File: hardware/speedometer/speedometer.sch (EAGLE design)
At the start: 123 parts, among them IC1 PIC32MX274F256DT-I_PT, IC10 24LC024SN, IC11 MAX16054AZT+T, IC12 TPS63001DRCT, IC13 TPS63002DRCT, IC2 CSTCE8M00G55-R0, IC3 BQ27441DRZR-G1A, IC7 BQ24075RGTT, IC8 NRF24L01P-T, IC9 CSTCE16M0V53-R0, J1 10104111-0001LF, J2 BAT, J3 CONUFL001-SMD-T, J4 Right_sens, J5 Right, J6 Left_sens, J7 Left, Q1 BC817, Q2 BC817, Q3 BC817, Q4 BC817

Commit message: Minor stuff
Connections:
- removed net UDB_ID: IC1.TMS/RPB5/USBID/RB5
- net USB_ID: now also IC1.TMS/RPB5/USBID/RB5
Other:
- note added: "Short to boot in bootloader mode"
- moved on the sheet: JP3, R14
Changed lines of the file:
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@@
 <text x="20.32" y="86.36" size="1.778" layer="91" font="vector" rot="R90">ESR &lt;= 3 Ohm</text>
 <text x="129.54" y="38.1" size="3.81" layer="91" font="vector">5V Tolerant</text>
+<text x="73.66" y="38.1" size="3.81" layer="91">Short to boot in
+bootloader mode</text>
 </plain>
 <instances>
@@
 <instance part="GND4" gate="1" x="63.5" y="55.88"/>
 <instance part="+3V4" gate="G$1" x="38.1" y="93.98" rot="R90"/>
-<instance part="+3V7" gate="G$1" x="38.1" y="73.66" rot="R90"/>
+<instance part="+3V7" gate="G$1" x="25.4" y="73.66" rot="R90"/>
 <instance part="+3V8" gate="G$1" x="231.14" y="106.68" rot="R270"/>
 <instance part="+3V9" gate="G$1" x="215.9" y="73.66" rot="R270"/>
@@
 <instance part="JP2" gate="A" x="149.86" y="27.94"/>
 <instance part="GND19" gate="1" x="139.7" y="17.78"/>
-<instance part="JP3" gate="G$1" x="121.92" y="27.94"/>
-<instance part="+3V14" gate="G$1" x="111.76" y="40.64"/>
-<instance part="R14" gate="G$1" x="104.14" y="22.86"/>
-<instance part="GND20" gate="1" x="96.52" y="17.78"/>
+<instance part="JP3" gate="G$1" x="109.22" y="27.94"/>
+<instance part="+3V14" gate="G$1" x="99.06" y="35.56"/>
+<instance part="R14" gate="G$1" x="91.44" y="22.86"/>
+<instance part="GND20" gate="1" x="83.82" y="17.78"/>
 </instances>
 <busses>
@@
 <segment>
 <pinref part="R14" gate="G$1" pin="1"/>
-<wire x1="99.06" y1="22.86" x2="96.52" y2="22.86" width="0.1524" layer="91"/>
-<wire x1="96.52" y1="22.86" x2="96.52" y2="20.32" width="0.1524" layer="91"/>
+<wire x1="86.36" y1="22.86" x2="83.82" y2="22.86" width="0.1524" layer="91"/>
+<wire x1="83.82" y1="22.86" x2="83.82" y2="20.32" width="0.1524" layer="91"/>
 <pinref part="GND20" gate="1" pin="GND"/>
 </segment>
@@
 <pinref part="+3V7" gate="G$1" pin="+3V3"/>
 <pinref part="IC1" gate="G$1" pin="AVDD"/>
-<wire x1="40.64" y1="73.66" x2="66.04" y2="73.66" width="0.1524" layer="91"/>
+<wire x1="27.94" y1="73.66" x2="66.04" y2="73.66" width="0.1524" layer="91"/>
 </segment>
 <segment>
@@
 <segment>
 <pinref part="JP3" gate="G$1" pin="1"/>
-<wire x1="119.38" y1="30.48" x2="114.3" y2="30.48" width="0.1524" layer="91"/>
-<wire x1="114.3" y1="30.48" x2="111.76" y2="30.48" width="0.1524" layer="91"/>
-<wire x1="111.76" y1="30.48" x2="111.76" y2="38.1" width="0.1524" layer="91"/>
+<wire x1="106.68" y1="30.48" x2="101.6" y2="30.48" width="0.1524" layer="91"/>
+<wire x1="101.6" y1="30.48" x2="99.06" y2="30.48" width="0.1524" layer="91"/>
+<wire x1="99.06" y1="30.48" x2="99.06" y2="33.02" width="0.1524" layer="91"/>
 <pinref part="+3V14" gate="G$1" pin="+3V3"/>
 </segment>
@@
 <label x="104.14" y="154.94" size="1.27" layer="95" font="vector" rot="R180" xref="yes"/>
 </segment>
-</net>
-<net name="UDB_ID" class="0">
 <segment>
 <pinref part="IC1" gate="G$1" pin="TMS/RPB5/USBID/RB5"/>
@@
 <segment>
 <pinref part="JP3" gate="G$1" pin="2"/>
-<wire x1="119.38" y1="27.94" x2="111.76" y2="27.94" width="0.1524" layer="91"/>
-<label x="93.98" y="27.94" size="1.27" layer="95" font="vector" rot="R180" xref="yes"/>
+<wire x1="106.68" y1="27.94" x2="99.06" y2="27.94" width="0.1524" layer="91"/>
+<label x="81.28" y="27.94" size="1.27" layer="95" font="vector" rot="R180" xref="yes"/>
 <pinref part="R14" gate="G$1" pin="2"/>
-<wire x1="111.76" y1="27.94" x2="93.98" y2="27.94" width="0.1524" layer="91"/>
-<wire x1="109.22" y1="22.86" x2="111.76" y2="22.86" width="0.1524" layer="91"/>
-<wire x1="111.76" y1="22.86" x2="111.76" y2="27.94" width="0.1524" layer="91"/>
-<junction x="111.76" y="27.94"/>
-</segment>
-</net>
+<wire x1="99.06" y1="27.94" x2="81.28" y2="27.94" width="0.1524" layer="91"/>
+<wire x1="96.52" y1="22.86" x2="99.06" y2="22.86" width="0.1524" layer="91"/>
+<wire x1="99.06" y1="22.86" x2="99.06" y2="27.94" width="0.1524" layer="91"/>
+<junction x="99.06" y="27.94"/>
+</segment>
+</net>

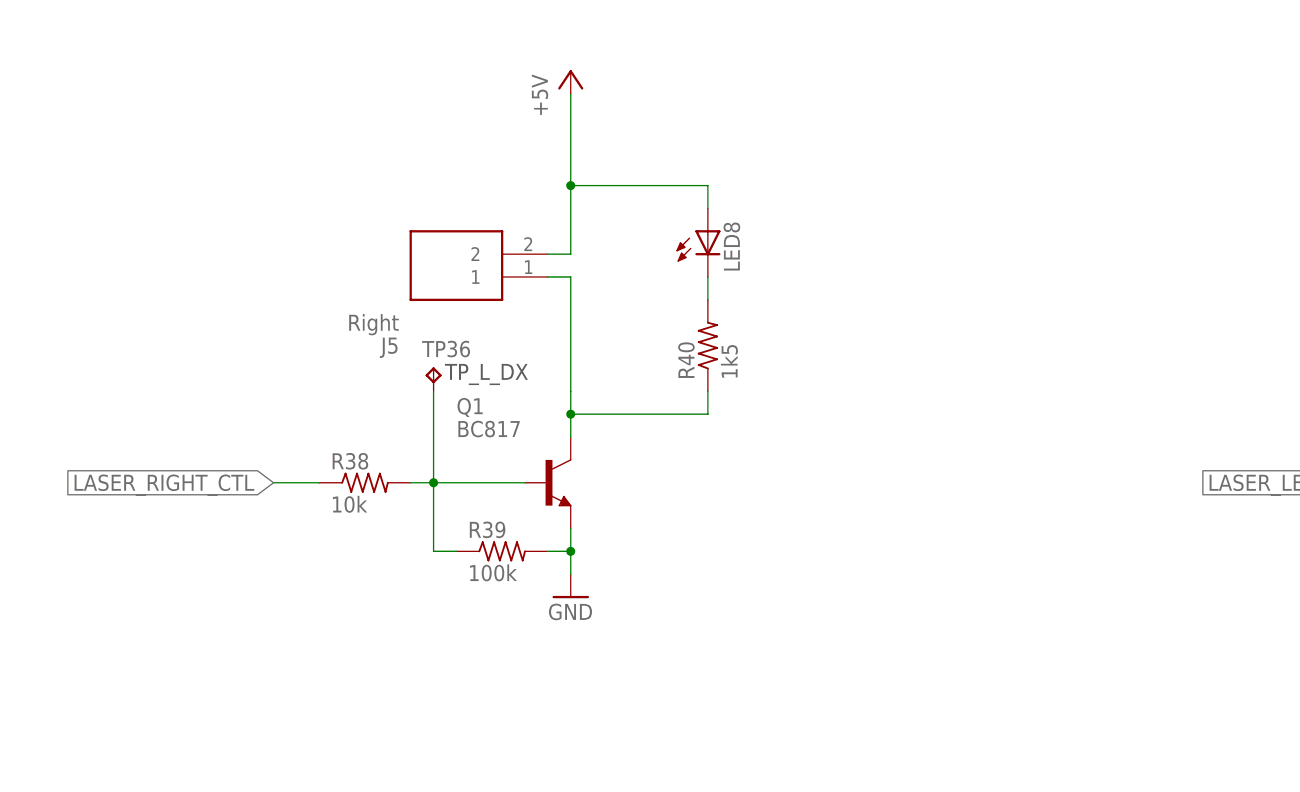
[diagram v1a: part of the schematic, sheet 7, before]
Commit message: Laser ctl logic added
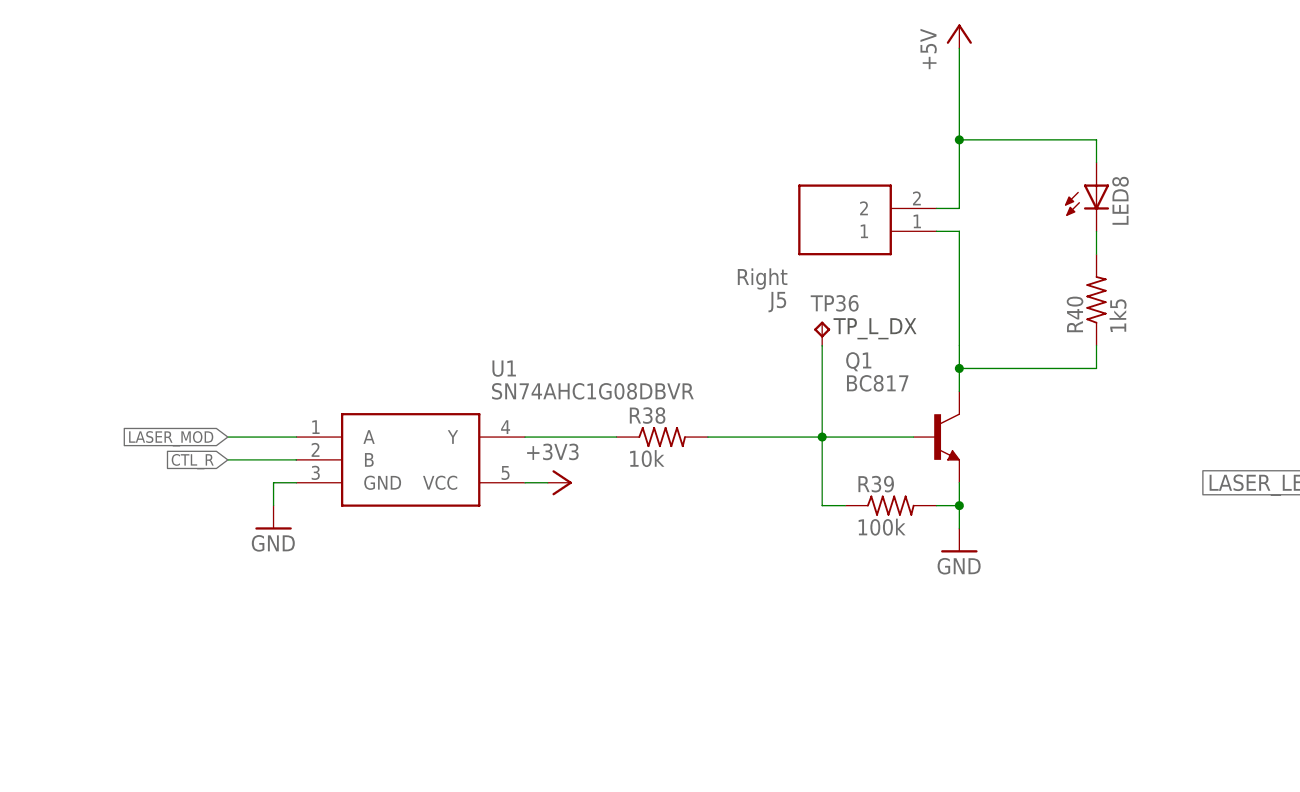
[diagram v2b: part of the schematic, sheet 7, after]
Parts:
- added U1: SN74AHC1G08DBVR, SN74AHC1G08DBVR:SN74AHC1G08DBVR
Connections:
- removed net LASER_RIGHT_CTL: R38.1
- new net LASER_MOD: IC1.RPC7/PMCS1/RC7, U1.A
- new net N$42: R38.1, U1.Y
- net +3V3: now also U1.VCC
- net CTL_R: now also U1.B
- net GND: now also U1.GND
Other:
- moved on the sheet: J5, LED8, Q1, R38, R39, R40, TP36
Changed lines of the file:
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@@
 <part name="R14" library="rcl" library_urn="urn:adsk.eagle:library:334" deviceset="R-US_" device="M0805" package3d_urn="urn:adsk.eagle:package:23556/1" value="10k"/>
 <part name="GND20" library="supply1" library_urn="urn:adsk.eagle:library:371" deviceset="GND" device=""/>
+<part name="U1" library="SN74AHC1G08DBVR" deviceset="SN74AHC1G08DBVR" device=""/>
+<part name="GND21" library="supply1" library_urn="urn:adsk.eagle:library:371" deviceset="GND" device=""/>
+<part name="+3V15" library="supply1" library_urn="urn:adsk.eagle:library:371" deviceset="+3V3" device=""/>
 </parts>
 <sheets>
@@
 </segment>
 </net>
+<net name="LASER_MOD" class="0">
+<segment>
+<pinref part="IC1" gate="G$1" pin="RPC7/PMCS1/RC7"/>
+<wire x1="66.04" y1="111.76" x2="53.34" y2="111.76" width="0.1524" layer="91"/>
+<label x="53.34" y="111.76" size="1.27" layer="95" font="vector" rot="R180" xref="yes"/>
+</segment>
+</net>
 </nets>
 </sheet>
@@
 <instances>
 <instance part="FRAME9" gate="G$1" x="0" y="0"/>
-<instance part="Q1" gate="G$1" x="66.04" y="114.3"/>
-<instance part="GND67" gate="1" x="68.58" y="101.6"/>
-<instance part="R38" gate="G$1" x="45.72" y="114.3"/>
-<instance part="R39" gate="G$1" x="60.96" y="106.68"/>
-<instance part="TP36" gate="G$1" x="53.34" y="127"/>
-<instance part="LED8" gate="G$1" x="83.82" y="142.24"/>
-<instance part="R40" gate="G$1" x="83.82" y="129.54" rot="R90"/>
-<instance part="J5" gate="G$1" x="66.04" y="137.16" rot="R180"/>
+<instance part="Q1" gate="G$1" x="109.22" y="119.38"/>
+<instance part="GND67" gate="1" x="111.76" y="106.68"/>
+<instance part="R38" gate="G$1" x="78.74" y="119.38"/>
+<instance part="R39" gate="G$1" x="104.14" y="111.76"/>
+<instance part="TP36" gate="G$1" x="96.52" y="132.08"/>
+<instance part="LED8" gate="G$1" x="127" y="147.32"/>
+<instance part="R40" gate="G$1" x="127" y="134.62" rot="R90"/>
+<instance part="J5" gate="G$1" x="109.22" y="142.24" rot="R180"/>
 <instance part="J4" gate="G$1" x="48.26" y="45.72" rot="R180"/>
 <instance part="GND66" gate="1" x="53.34" y="40.64"/>
@@
 <instance part="J6" gate="G$1" x="172.72" y="45.72" rot="R180"/>
 <instance part="GND68" gate="1" x="177.8" y="40.64"/>
-<instance part="P+2" gate="1" x="68.58" y="160.02"/>
+<instance part="P+2" gate="1" x="111.76" y="165.1"/>
 <instance part="P+3" gate="1" x="193.04" y="160.02"/>
 <instance part="P+4" gate="1" x="53.34" y="71.12"/>
@@
 <instance part="R25" gate="G$1" x="218.44" y="60.96" rot="R90"/>
 <instance part="+3V6" gate="G$1" x="218.44" y="71.12"/>
+<instance part="U1" gate="G$1" x="38.1" y="119.38"/>
+<instance part="GND21" gate="1" x="35.56" y="109.22"/>
+<instance part="+3V15" gate="G$1" x="68.58" y="114.3" rot="R270"/>
 </instances>
 <busses>
@@
 <segment>
 <pinref part="Q1" gate="G$1" pin="C"/>
-<wire x1="68.58" y1="119.38" x2="68.58" y2="121.92" width="0.1524" layer="91"/>
-<wire x1="68.58" y1="121.92" x2="68.58" y2="124.46" width="0.1524" layer="91"/>
-<wire x1="68.58" y1="121.92" x2="83.82" y2="121.92" width="0.1524" layer="91"/>
-<junction x="68.58" y="121.92"/>
+<wire x1="111.76" y1="124.46" x2="111.76" y2="127" width="0.1524" layer="91"/>
+<wire x1="111.76" y1="127" x2="111.76" y2="129.54" width="0.1524" layer="91"/>
+<wire x1="111.76" y1="127" x2="127" y2="127" width="0.1524" layer="91"/>
+<junction x="111.76" y="127"/>
 <pinref part="R40" gate="G$1" pin="1"/>
-<wire x1="83.82" y1="121.92" x2="83.82" y2="124.46" width="0.1524" layer="91"/>
+<wire x1="127" y1="127" x2="127" y2="129.54" width="0.1524" layer="91"/>
 <pinref part="J5" gate="G$1" pin="1"/>
-<wire x1="66.04" y1="137.16" x2="68.58" y2="137.16" width="0.1524" layer="91"/>
-<wire x1="68.58" y1="137.16" x2="68.58" y2="124.46" width="0.1524" layer="91"/>
+<wire x1="109.22" y1="142.24" x2="111.76" y2="142.24" width="0.1524" layer="91"/>
+<wire x1="111.76" y1="142.24" x2="111.76" y2="129.54" width="0.1524" layer="91"/>
 </segment>
 </net>
@@
 <pinref part="Q1" gate="G$1" pin="E"/>
 <pinref part="GND67" gate="1" pin="GND"/>
-<wire x1="68.58" y1="109.22" x2="68.58" y2="106.68" width="0.1524" layer="91"/>
+<wire x1="111.76" y1="114.3" x2="111.76" y2="111.76" width="0.1524" layer="91"/>
 <pinref part="R39" gate="G$1" pin="2"/>
-<wire x1="68.58" y1="106.68" x2="68.58" y2="104.14" width="0.1524" layer="91"/>
-<wire x1="66.04" y1="106.68" x2="68.58" y2="106.68" width="0.1524" layer="91"/>
-<junction x="68.58" y="106.68"/>
+<wire x1="111.76" y1="111.76" x2="111.76" y2="109.22" width="0.1524" layer="91"/>
+<wire x1="109.22" y1="111.76" x2="111.76" y2="111.76" width="0.1524" layer="91"/>
+<junction x="111.76" y="111.76"/>
 </segment>
 <segment>
@@
 <junction x="218.44" y="38.1"/>
 </segment>
+<segment>
+<pinref part="U1" gate="G$1" pin="GND"/>
+<wire x1="38.1" y1="114.3" x2="35.56" y2="114.3" width="0.1524" layer="91"/>
+<wire x1="35.56" y1="114.3" x2="35.56" y2="111.76" width="0.1524" layer="91"/>
+<pinref part="GND21" gate="1" pin="GND"/>
+</segment>
 </net>
 <net name="N$39" class="0">
 <segment>
 <pinref part="R39" gate="G$1" pin="1"/>
-<wire x1="55.88" y1="106.68" x2="53.34" y2="106.68" width="0.1524" layer="91"/>
-<wire x1="53.34" y1="106.68" x2="53.34" y2="114.3" width="0.1524" layer="91"/>
+<wire x1="99.06" y1="111.76" x2="96.52" y2="111.76" width="0.1524" layer="91"/>
+<wire x1="96.52" y1="111.76" x2="96.52" y2="119.38" width="0.1524" layer="91"/>
 <pinref part="R38" gate="G$1" pin="2"/>
-<wire x1="53.34" y1="114.3" x2="50.8" y2="114.3" width="0.1524" layer="91"/>
+<wire x1="96.52" y1="119.38" x2="83.82" y2="119.38" width="0.1524" layer="91"/>
 <pinref part="Q1" gate="G$1" pin="B"/>
-<wire x1="53.34" y1="114.3" x2="63.5" y2="114.3" width="0.1524" layer="91"/>
-<junction x="53.34" y="114.3"/>
+<wire x1="96.52" y1="119.38" x2="106.68" y2="119.38" width="0.1524" layer="91"/>
+<junction x="96.52" y="119.38"/>
 <pinref part="TP36" gate="G$1" pin="TP"/>
-<wire x1="53.34" y1="124.46" x2="53.34" y2="114.3" width="0.1524" layer="91"/>
-</segment>
-</net>
-<net name="LASER_RIGHT_CTL" class="0">
-<segment>
-<pinref part="R38" gate="G$1" pin="1"/>
-<wire x1="40.64" y1="114.3" x2="35.56" y2="114.3" width="0.1524" layer="91"/>
-<label x="35.56" y="114.3" size="1.778" layer="95" rot="R180" xref="yes"/>
+<wire x1="96.52" y1="129.54" x2="96.52" y2="119.38" width="0.1524" layer="91"/>
 </segment>
 </net>
@@
 <pinref part="LED8" gate="G$1" pin="C"/>
 <pinref part="R40" gate="G$1" pin="2"/>
-<wire x1="83.82" y1="137.16" x2="83.82" y2="134.62" width="0.1524" layer="91"/>
+<wire x1="127" y1="142.24" x2="127" y2="139.7" width="0.1524" layer="91"/>
 </segment>
 </net>
@@
 <pinref part="+3V6" gate="G$1" pin="+3V3"/>
 <wire x1="218.44" y1="66.04" x2="218.44" y2="68.58" width="0.1524" layer="91"/>
+</segment>
+<segment>
+<pinref part="U1" gate="G$1" pin="VCC"/>
+<wire x1="63.5" y1="114.3" x2="66.04" y2="114.3" width="0.1524" layer="91"/>
+<pinref part="+3V15" gate="G$1" pin="+3V3"/>
 </segment>
 </net>
@@
 <segment>
 <pinref part="LED8" gate="G$1" pin="A"/>
-<wire x1="83.82" y1="144.78" x2="83.82" y2="147.32" width="0.1524" layer="91"/>
-<wire x1="83.82" y1="147.32" x2="68.58" y2="147.32" width="0.1524" layer="91"/>
-<wire x1="68.58" y1="147.32" x2="68.58" y2="157.48" width="0.1524" layer="91"/>
-<junction x="68.58" y="147.32"/>
+<wire x1="127" y1="149.86" x2="127" y2="152.4" width="0.1524" layer="91"/>
+<wire x1="127" y1="152.4" x2="111.76" y2="152.4" width="0.1524" layer="91"/>
+<wire x1="111.76" y1="152.4" x2="111.76" y2="162.56" width="0.1524" layer="91"/>
+<junction x="111.76" y="152.4"/>
 <pinref part="J5" gate="G$1" pin="2"/>
-<wire x1="66.04" y1="139.7" x2="68.58" y2="139.7" width="0.1524" layer="91"/>
-<wire x1="68.58" y1="139.7" x2="68.58" y2="147.32" width="0.1524" layer="91"/>
+<wire x1="109.22" y1="144.78" x2="111.76" y2="144.78" width="0.1524" layer="91"/>
+<wire x1="111.76" y1="144.78" x2="111.76" y2="152.4" width="0.1524" layer="91"/>
 <pinref part="P+2" gate="1" pin="+5V"/>
 </segment>
@@
 </segment>
 </net>
+<net name="LASER_MOD" class="0">
+<segment>
+<pinref part="U1" gate="G$1" pin="A"/>
+<wire x1="38.1" y1="119.38" x2="30.48" y2="119.38" width="0.1524" layer="91"/>
+<label x="30.48" y="119.38" size="1.27" layer="95" font="vector" rot="R180" xref="yes"/>
+</segment>
+</net>
+<net name="CTL_R" class="0">
+<segment>
+<pinref part="U1" gate="G$1" pin="B"/>
+<wire x1="38.1" y1="116.84" x2="30.48" y2="116.84" width="0.1524" layer="91"/>
+<label x="30.48" y="116.84" size="1.27" layer="95" font="vector" rot="R180" xref="yes"/>
+</segment>
+</net>
+<net name="N$42" class="0">
+<segment>
+<pinref part="U1" gate="G$1" pin="Y"/>
+<pinref part="R38" gate="G$1" pin="1"/>
+<wire x1="63.5" y1="119.38" x2="73.66" y2="119.38" width="0.1524" layer="91"/>
+</segment>
+</net>

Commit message: notes added
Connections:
- net VDD: now also IC1.VBUS
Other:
- note added: "INT2"
- note added: "INT3"
- note added: "OC1"
